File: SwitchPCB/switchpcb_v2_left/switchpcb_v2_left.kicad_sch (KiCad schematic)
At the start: 77 parts, among them J1 Conn_01x08, Q1 2N7002, Q10 2N7002, Q11 BC847, Q12 2N7002, Q13 BC847, Q14 2N7002, Q15 BC847, Q16 2N7002, Q17 BC847, Q18 BC847, Q19 2N7002, Q2 2N7002, Q20 2N7002, Q21 BC847, Q22 BC847, Q23 2N7002, Q24 2N7002, Q3 BC847, Q4 BC847, Q5 BC847, Q6 2N7002, Q7 BC847, Q8 2N7002, Q9 BC847, SW1 Lehle_Switch, SW2 Lehle_Switch, SW3 Lehle_Switch, SW4 Lehle_Switch, U1 74HC595, U2 74HC595

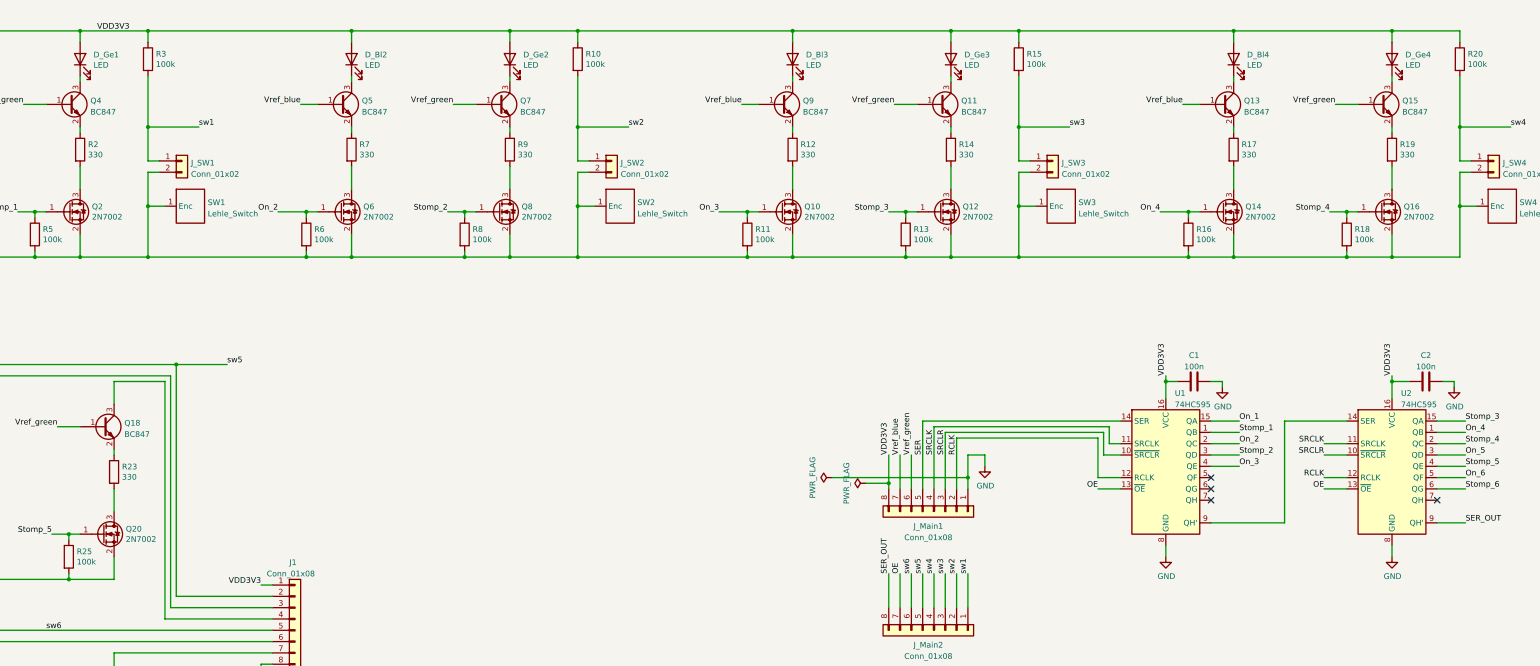
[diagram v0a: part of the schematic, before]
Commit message: Changed switch pcb left to 9V led supply
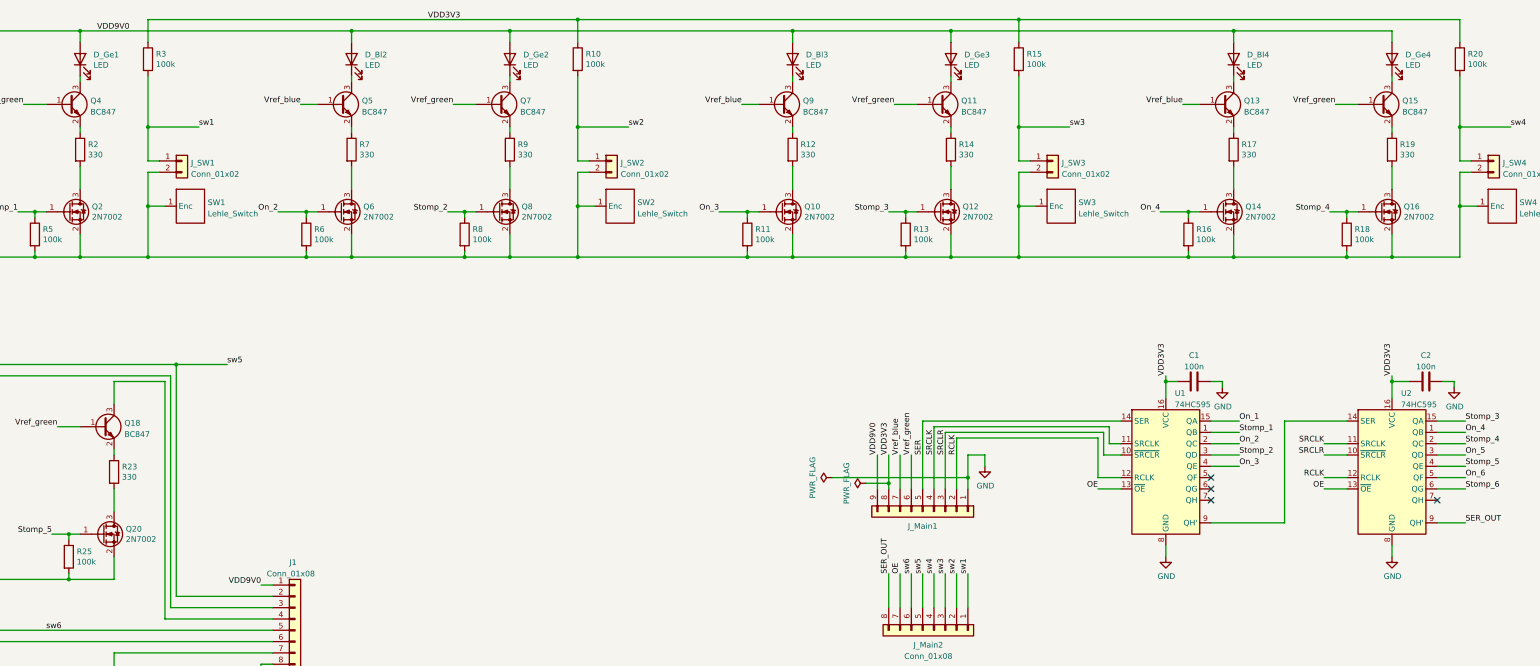
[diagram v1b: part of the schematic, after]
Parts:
- removed J_Main1: Conn_01x08, Connector_JST:JST_PH_B8B-PH-K_1x08_P2.00mm_Vertical, symbol Connector_Generic:Conn_01x08
- added J_Main1: (no value), symbol Connector_Generic:Conn_01x09
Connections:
- net GND: now also J_Main1.1 (Pin_1)
- net RCLK: now also J_Main1.2 (Pin_2)
- net SER: now also J_Main1.5 (Pin_5)
- net SRCLK: now also J_Main1.4 (Pin_4)
- net SRCLR: now also J_Main1.3 (Pin_3)
- net VDD3V3: now also J_Main1.8 (Pin_8); no longer D_Bl1.2 (A), D_Bl2.2 (A), D_Bl3.2 (A), D_Bl4.2 (A), D_Ge1.2 (A), D_Ge2.2 (A), D_Ge3.2 (A), D_Ge4.2 (A), J1.1 (Pin_1)
- net Vref_blue: now also J_Main1.7 (Pin_7)
- net Vref_green: now also J_Main1.6 (Pin_6)
- new net VDD9V0: D_Bl1.2 (A), D_Bl2.2 (A), D_Bl3.2 (A), D_Bl4.2 (A), D_Ge1.2 (A), D_Ge2.2 (A), D_Ge3.2 (A), D_Ge4.2 (A), J1.1 (Pin_1), J_Main1.9 (Pin_9)

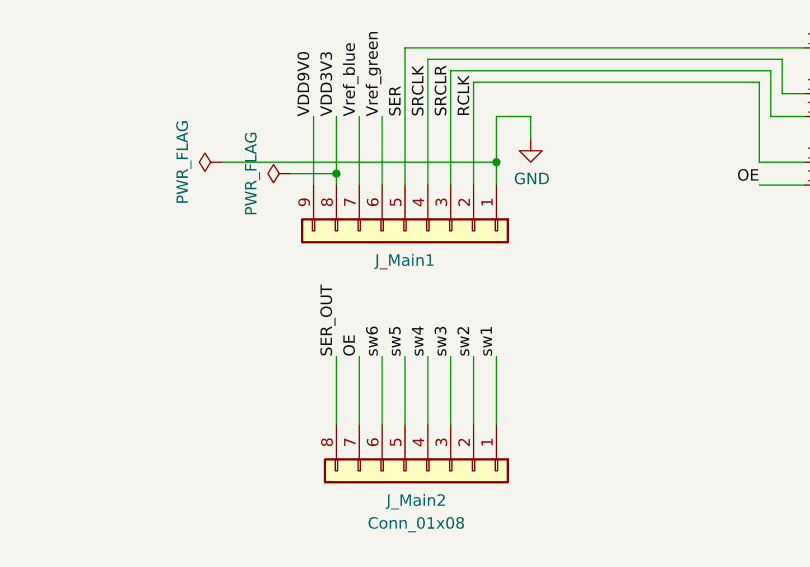
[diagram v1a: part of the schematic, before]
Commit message: 3D models and fixed pcbs
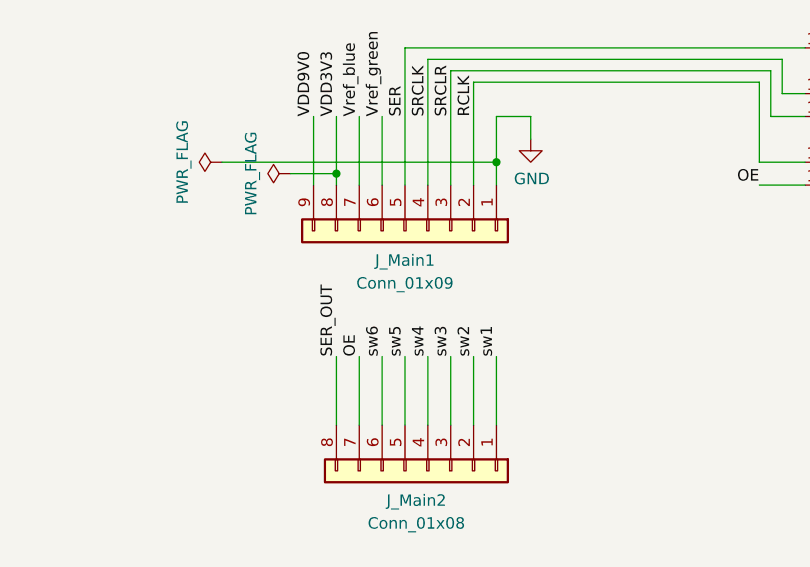
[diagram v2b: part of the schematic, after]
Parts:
- J_Main1: value (none) -> Conn_01x09; footprint (none) -> Connector_JST:JST_PH_B9B-PH-K_1x09_P2.00mm_Vertical
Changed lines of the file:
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@@
     (pin "3")
   )
-  (symbol (lib_id "power:GND") (at 21.59 96.52 0) (unit 1)
+  (symbol (lib_name "GND_3") (lib_id "power:GND") (at 21.59 96.52 0) (unit 1)
     (in_bom yes) (on_board yes)
     (property "Reference" "#PWR0102" (id 0) (at 21.59 102.87 0)
@@
     (pin "1")
   )
-  (symbol (lib_id "power:GND") (at 375.92 162.56 0) (unit 1)
+  (symbol (lib_name "GND_8") (lib_id "power:GND") (at 375.92 162.56 0) (unit 1)
     (in_bom yes) (on_board yes)
     (property "Reference" "#PWR0104" (id 0) (at 375.92 168.91 0)
@@
     (pin "3")
   )
-  (symbol (lib_id "power:GND") (at 121.92 189.23 0) (unit 1)
+  (symbol (lib_name "GND_4") (lib_id "power:GND") (at 121.92 189.23 0) (unit 1)
     (in_bom yes) (on_board yes)
     (property "Reference" "#PWR01" (id 0) (at 121.92 195.58 0)
@@
     (pin "9")
   )
-  (symbol (lib_id "power:GND") (at 284.48 142.24 0) (unit 1)
+  (symbol (lib_name "GND_6") (lib_id "power:GND") (at 284.48 142.24 0) (unit 1)
     (in_bom yes) (on_board yes)
     (property "Reference" "#PWR03" (id 0) (at 284.48 148.59 0)
@@
     (pin "3")
   )
-  (symbol (lib_id "power:PWR_FLAG") (at 250.19 144.78 90) (unit 1)
+  (symbol (lib_name "PWR_FLAG_1") (lib_id "power:PWR_FLAG") (at 250.19 144.78 90) (unit 1)
     (in_bom yes) (on_board yes)
     (property "Reference" "#FLG0101" (id 0) (at 248.285 144.78 0)
@@
     (pin "1")
   )
-  (symbol (lib_id "power:GND") (at 29.21 233.68 0) (unit 1)
+  (symbol (lib_name "GND_1") (lib_id "power:GND") (at 29.21 233.68 0) (unit 1)
     (in_bom yes) (on_board yes)
     (property "Reference" "#PWR02" (id 0) (at 29.21 240.03 0)
@@
     (in_bom yes) (on_board yes) (fields_autoplaced)
     (property "Reference" "J_Main1" (id 0) (at 270.51 155.7004 90))
-    (property "Value" "" (id 1) (at 270.51 158.2373 90))
-    (property "Footprint" "" (id 2) (at 270.51 152.4 0)
+    (property "Value" "Conn_01x09" (id 1) (at 270.51 158.2373 90))
+    (property "Footprint" "Connector_JST:JST_PH_B9B-PH-K_1x09_P2.00mm_Vertical" (id 2) (at 270.51 152.4 0)
       (effects (font (size 1.27 1.27)) hide)
     )
@@
     (pin "2")
   )
-  (symbol (lib_id "power:GND") (at 29.21 168.91 0) (unit 1)
+  (symbol (lib_name "GND_2") (lib_id "power:GND") (at 29.21 168.91 0) (unit 1)
     (in_bom yes) (on_board yes)
     (property "Reference" "#PWR0101" (id 0) (at 29.21 175.26 0)
@@
     (pin "1")
   )
-  (symbol (lib_id "power:GND") (at 325.12 162.56 0) (unit 1)
+  (symbol (lib_name "GND_7") (lib_id "power:GND") (at 325.12 162.56 0) (unit 1)
     (in_bom yes) (on_board yes)
     (property "Reference" "#PWR0103" (id 0) (at 325.12 168.91 0)
@@
     (pin "2")
   )
-  (symbol (lib_id "power:GND") (at 337.82 124.46 0) (unit 1)
+  (symbol (lib_name "GND_5") (lib_id "power:GND") (at 337.82 124.46 0) (unit 1)
     (in_bom yes) (on_board yes)
     (property "Reference" "#PWR04" (id 0) (at 337.82 130.81 0)

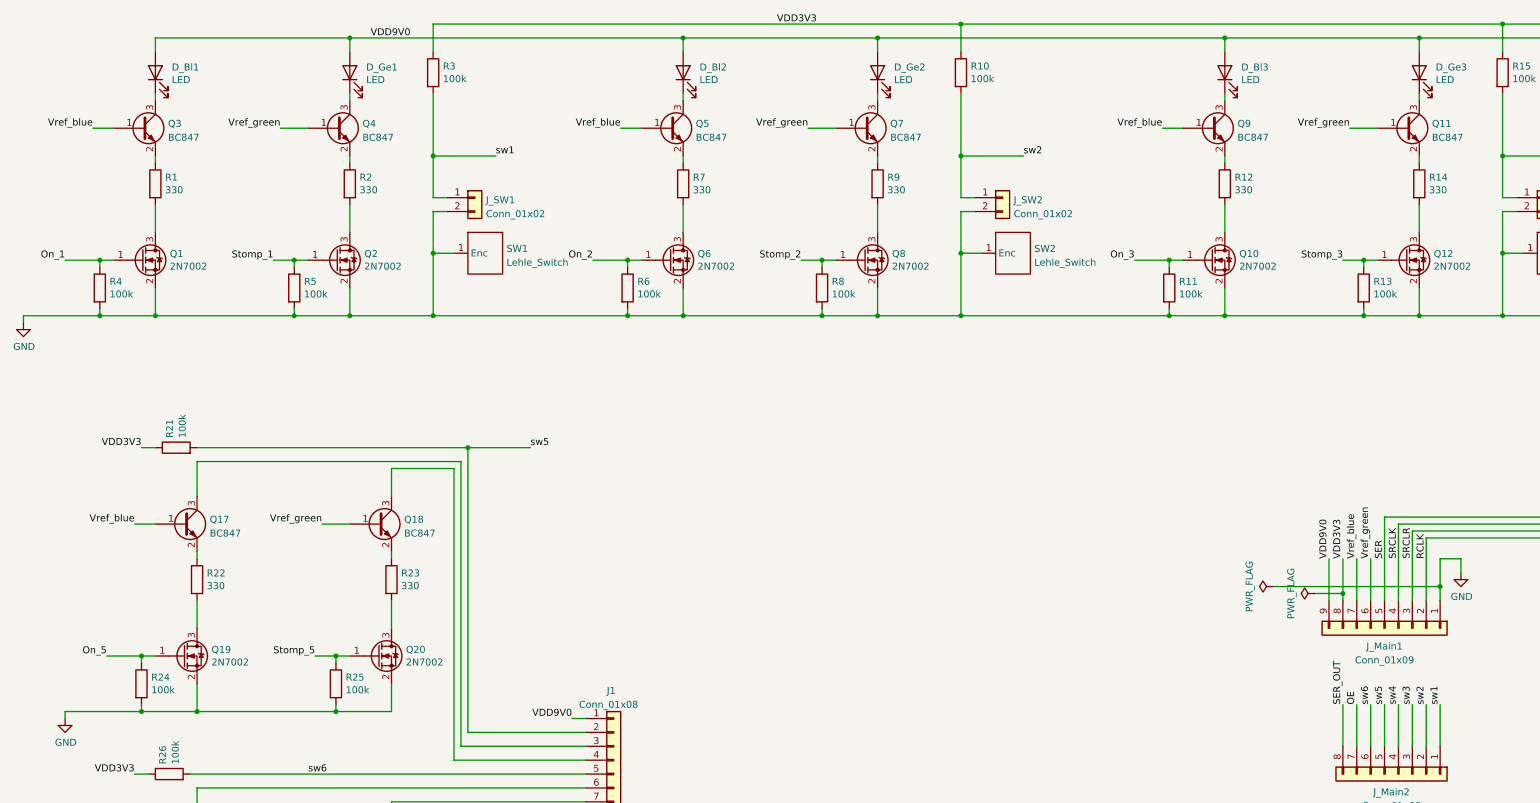
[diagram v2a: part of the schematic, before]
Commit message: Changed switch left to 3 switches
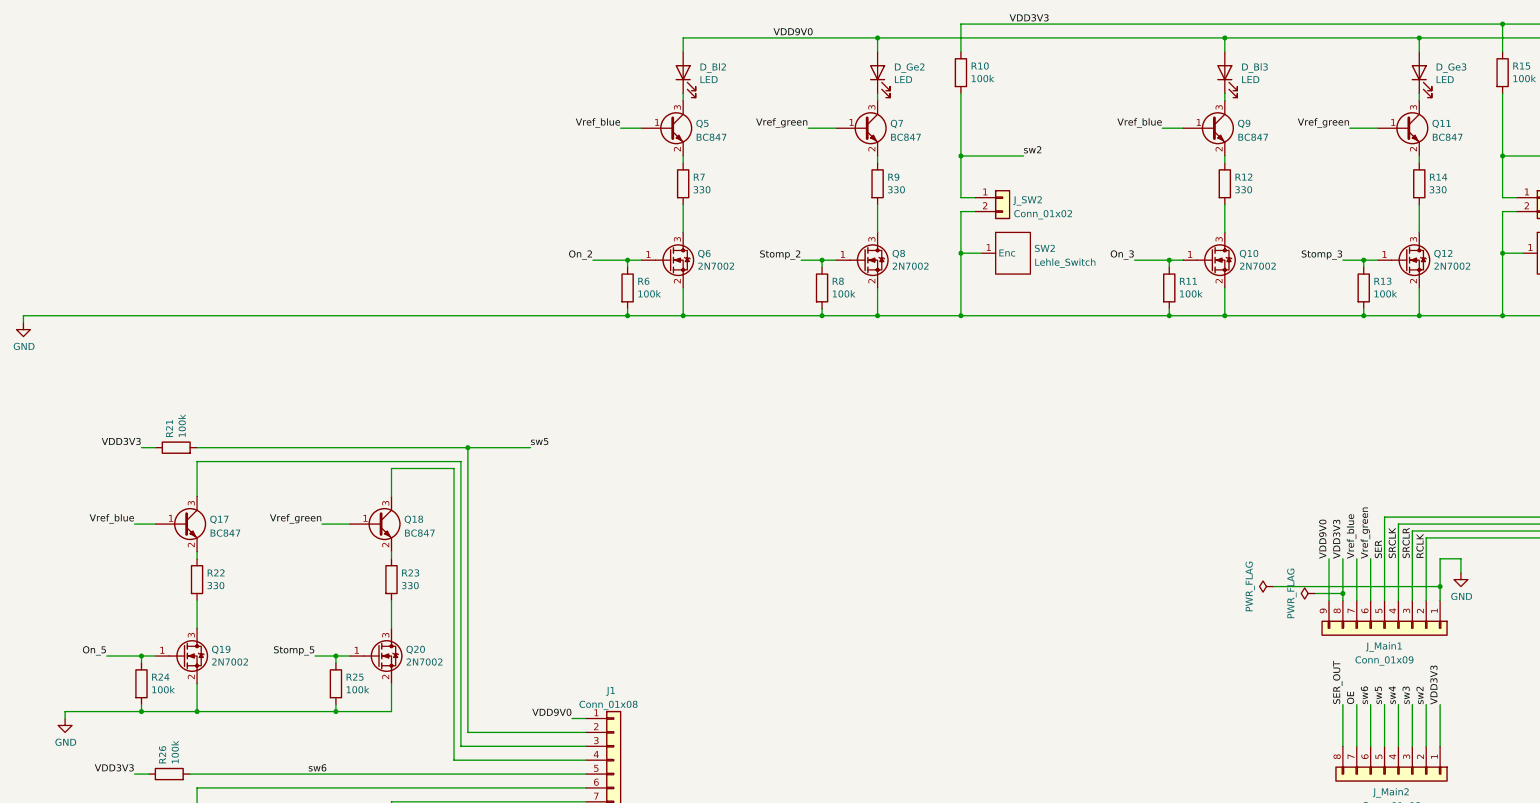
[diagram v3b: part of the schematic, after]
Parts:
- removed D_Bl1, D_Ge1: LED, LED_THT:LED_D3.0mm, symbol Device:LED
- removed J_SW1: Conn_01x02, Connector_JST:JST_PH_B2B-PH-K_1x02_P2.00mm_Vertical, symbol Connector_Generic:Conn_01x02
- removed Q1, Q2: 2N7002, Package_TO_SOT_SMD:SOT-23, symbol Transistor_FET:2N7002
- removed Q3, Q4: BC847, Package_TO_SOT_SMD:SOT-23, symbol Transistor_BJT:BC847
- removed R1, R2: 330, Resistor_SMD:R_1206_3216Metric_Pad1.30x1.75mm_HandSolder, symbol Device:R
- removed R3, R4, R5: 100k, Resistor_SMD:R_1206_3216Metric_Pad1.30x1.75mm_HandSolder, symbol Device:R
- removed SW1: Lehle_Switch, KiCad_Libs:LehleSwitch, symbol KiCad_Libs:Lehle_Switch
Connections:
- net sw1 is gone; now on net VDD3V3: J_Main2.1 (Pin_1)
